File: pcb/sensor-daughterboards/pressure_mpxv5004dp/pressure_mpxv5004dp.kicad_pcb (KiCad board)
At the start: 2 copper layers, 42 x 25 mm, 13 parts, among them J1 0.1" female header, bottom en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, J2 0.1" female header, bottom en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, U1 MPXV5004DP

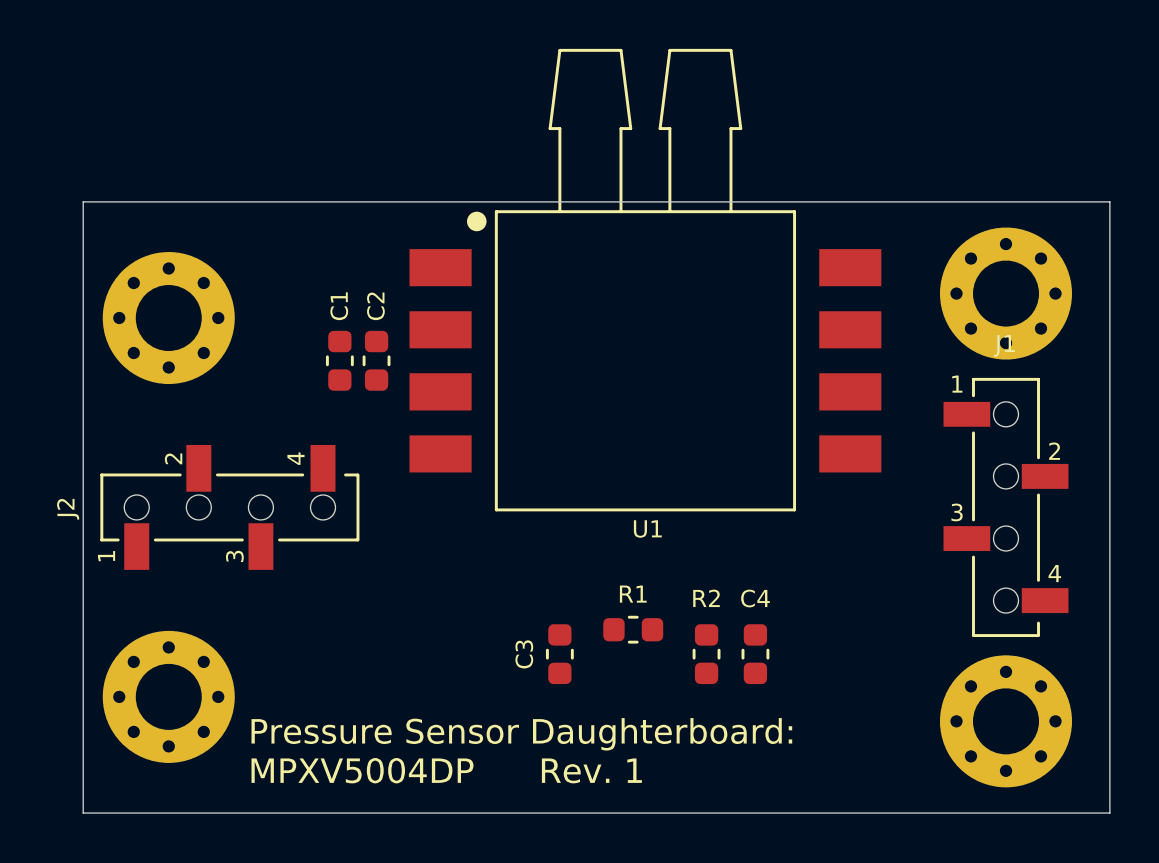
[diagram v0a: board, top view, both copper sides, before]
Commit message: Pressure daughterboard
Library references to RespiraWorks_Std
Removed unnecessary 10nF cap
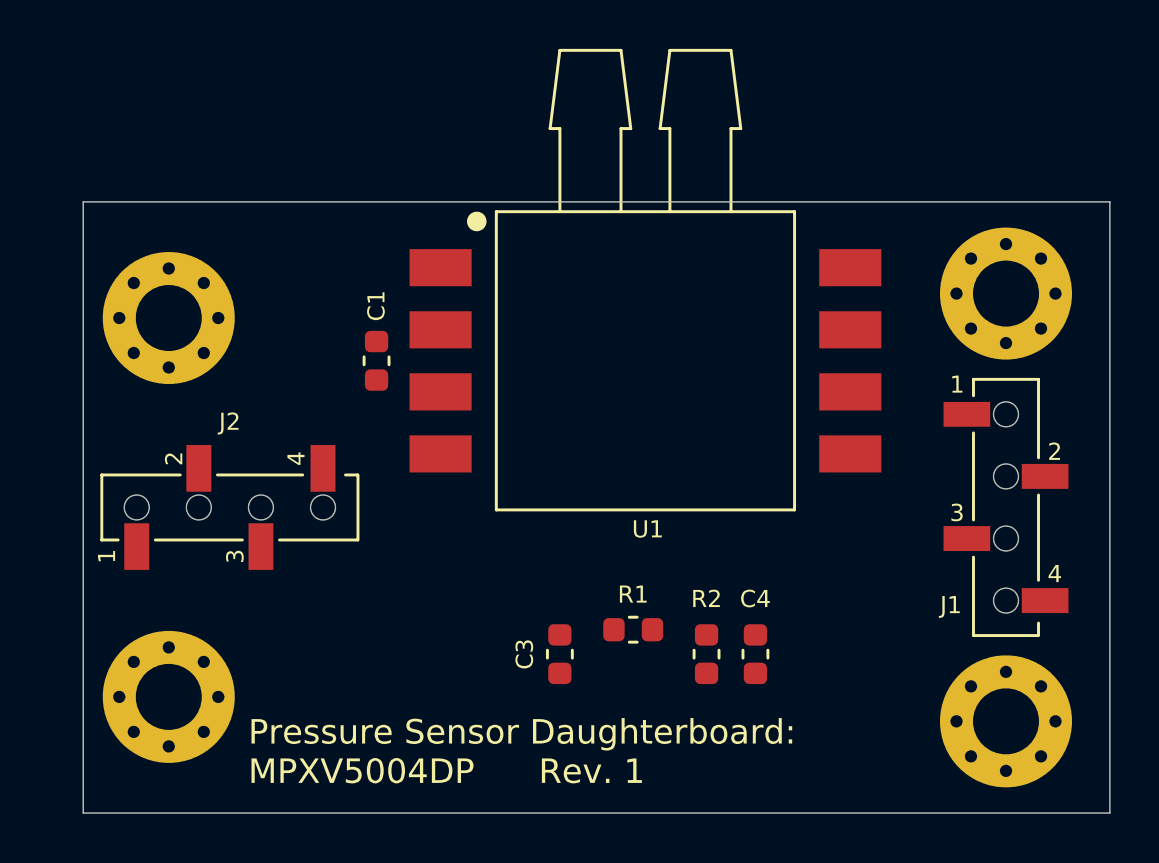
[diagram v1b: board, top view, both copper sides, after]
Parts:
- removed C2: 10nF, RespiraWorks_Std:C_0603_1608Metric
- H1, H2, H3, H4: footprint MountingHole:MountingHole_2.7mm_M2.5_Pad_Via -> RespiraWorks_Std:MountingHole_2.7mm_M2.5_Pad_Via
- J1, J2: value 0.1" female header, bottom entry -> Main board connections (bottom entry)
- moved C1 1.50 mm to (131.0, 84.0)
